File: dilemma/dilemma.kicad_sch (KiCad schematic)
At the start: 64 parts, among them J1 S3B-PH-SM4-TB(LF)(SN), J2 Serial, J3 BATTERY_CONN_DEANS, J5 S3B-PH-SM4-TB(LF)(SN), J7 trackball, SW1 SW_Push, SW10 SW_Push, SW11 SW_Push, SW12 SW_Push, SW13 SW_Push, SW14 SW_Push, SW15 SW_Push, SW16 SW_Push, SW17 SW_Push, SW2 SW_Push, SW26 SW_SPST, SW3 SW_Push, SW37 SW_SPST, SW4 SW_Push, SW5 SW_Push, SW6 SW_Push, SW7 SW_Push, SW8 SW_Push, SW9 SW_Push, U2 eliteC

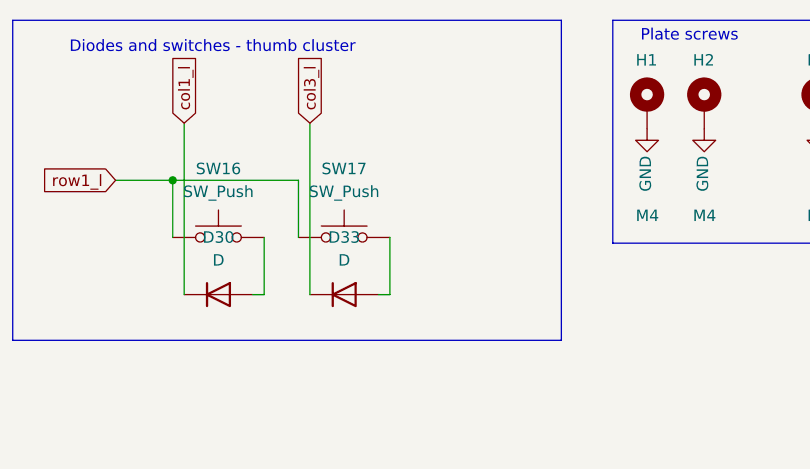
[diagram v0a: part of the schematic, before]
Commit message: added third thumb key in schematic and pcb layout
firmware not touched yet, case and supporting objects not touched yet, gerbers expored in the dilemma subfolder
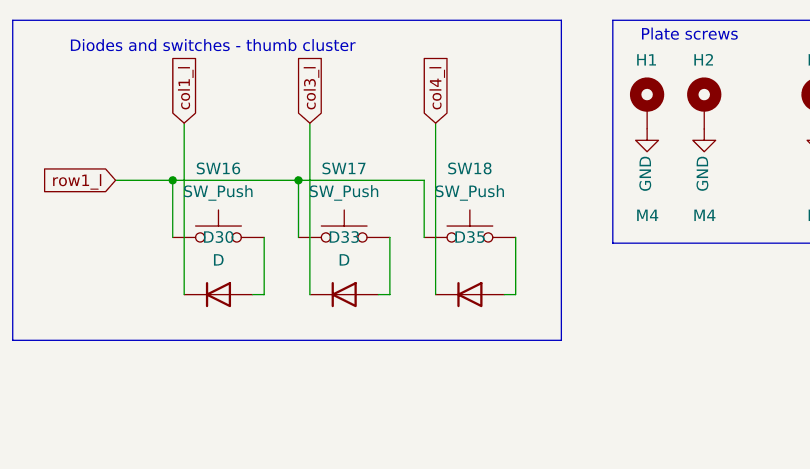
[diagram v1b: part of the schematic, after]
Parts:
- added D35: (no value), symbol Device:D
- added SW18: SW_Push, footprints:SW_MX_choc, symbol Switch:SW_Push
- D10, D13, D14, D15, D18, D19, D20, D24, D25, D26, D3, D30, D33, D4, D5, D8, D9: footprint local-libraries:D_1206_handsolder_reversible -> (none)
- SW1, SW10, SW11, SW12, SW13, SW14, SW15, SW16, SW17, SW2, SW3, SW4, SW5, SW6, SW7, SW8, SW9: footprint local-libraries:SW_MX_choc -> footprints:SW_MX_choc
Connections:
- net col4_l: now also D35.1 (K)
- net row1_l: now also SW18.1
- new net: D35.2 (A), SW18.2
